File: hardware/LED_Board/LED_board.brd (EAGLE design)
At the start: 50 x 23 mm, 115 parts, among them J2 QWIIC_RIGHT_ANGLE, U1 IS31FL3731-SALS2

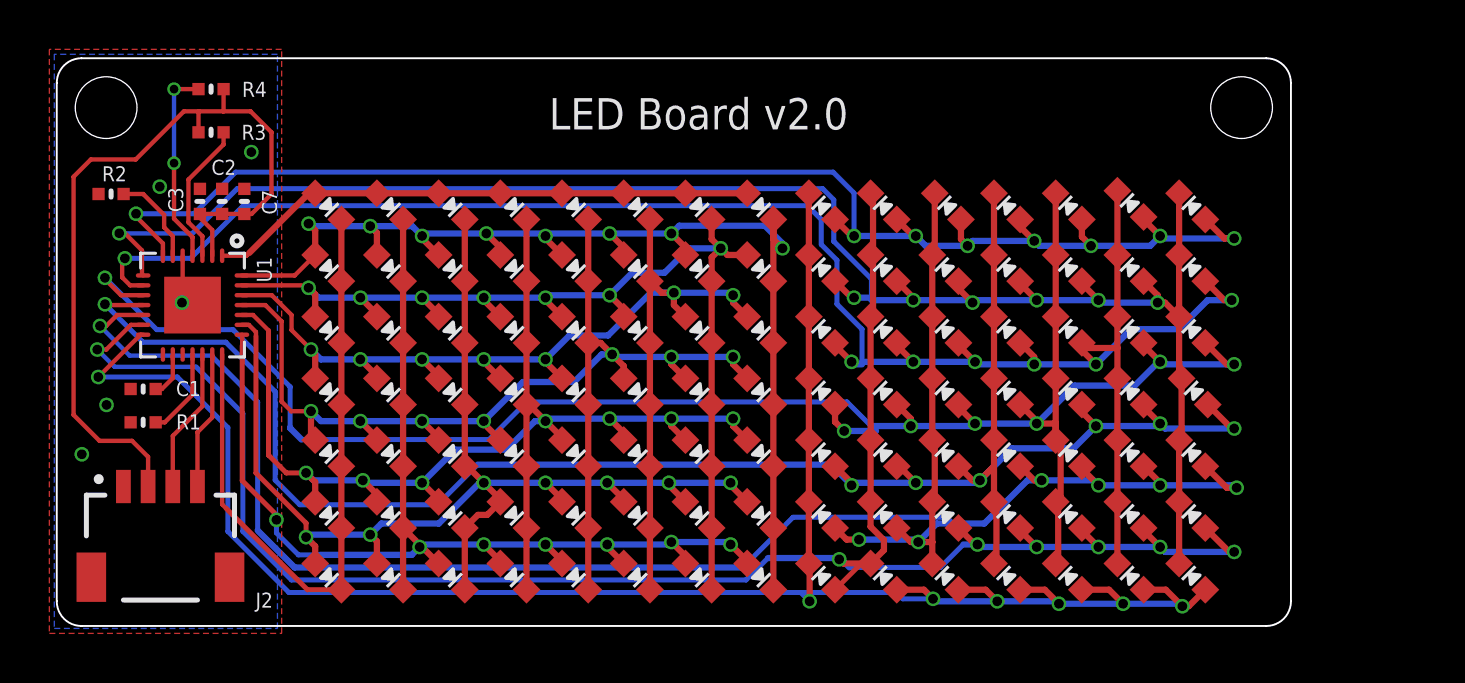
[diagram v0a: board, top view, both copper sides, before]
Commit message: LED board updated to v2.1
- Changed 0603 LEDs to 0402
- Arranged LEDs in grid of 3 x 2.5 mm spacing
- Increased board width from 50 to 55mm to accommodate spacing
- Rerouted all traces to LEDs again for new spacing (needs to be verified; v2.0 worked)
- ERC/DRC done
- Added BOM
- Updated gerbers, renders, schematic, dimensions
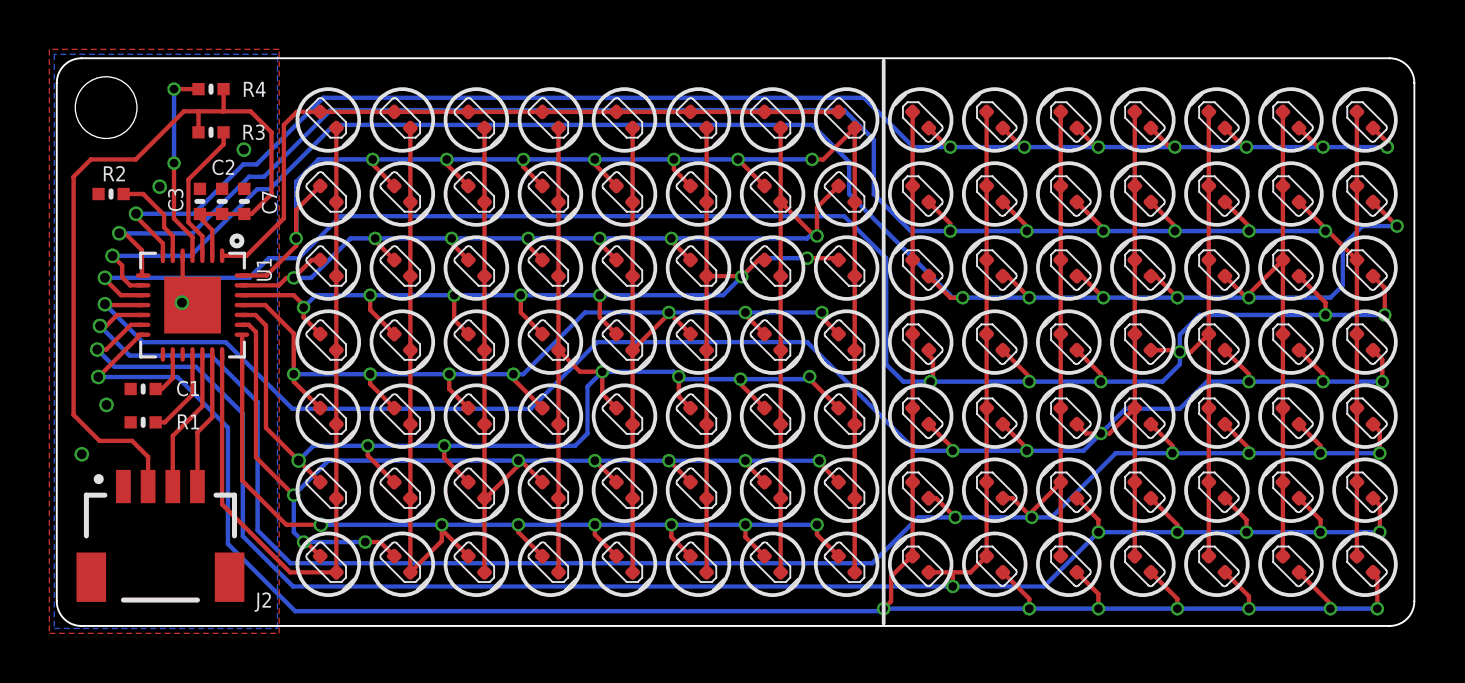
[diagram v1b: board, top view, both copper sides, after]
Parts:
- removed C1-2, C1-3, C1-4, C1-5, C1-6, C1-7, C1-8, C2-10, C2-11, C2-12, C2-13, C2-14, C2-15, C2-2, C2-3, C2-4, C2-5, C2-6, C2-7, C2-8, C2-9, C3-10, C3-11, C3-12, C3-13, C3-14, C3-15, C3-2, C3-3, C3-4, C3-5, C3-6, C3-7, C3-8, C3-9, C4-10, C4-11, C4-12, C4-13, C4-14, C4-15, C4-2, C4-3, C4-4, C4-5, C4-6, C4-7, C4-8, C4-9, C5-10, C5-11, C5-12, C5-13, C5-14, C5-15, C5-2, C5-3, C5-4, C5-5, C5-6, C5-7, C5-8, C5-9, C6-10, C6-11, C6-12, C6-13, C6-14, C6-15, C6-2, C6-3, C6-4, C6-5, C6-6, C6-7, C6-8, C6-9, C7-10, C7-11, C7-12, C7-13, C7-14, C7-15, C7-2, C7-3, C7-4, C7-5, C7-6, C7-7, C7-8, C7-9, C8-10, C8-11, C8-12, C8-13, C8-14, C8-15, C8-2, C8-3, C8-4, C8-5, C8-6, C8-7, C8-8, C8-9: (no value), microbuilder:CHIPLED_0603_NOOUTLINE
- added LED1, LED10, LED100, LED101, LED102, LED103, LED104, LED105, LED11, LED12, LED13, LED14, LED15, LED16, LED17, LED18, LED19, LED2, LED20, LED21, LED22, LED23, LED24, LED25, LED26, LED27, LED28, LED29, LED3, LED30, LED31, LED32, LED33, LED34, LED35, LED36, LED37, LED38, LED39, LED4, LED40, LED41, LED42, LED43, LED44, LED45, LED46, LED47, LED48, LED49, LED5, LED50, LED51, LED52, LED53, LED54, LED55, LED56, LED57, LED58, LED59, LED6, LED60, LED61, LED62, LED63, LED64, LED65, LED66, LED67, LED68, LED69, LED7, LED70, LED71, LED72, LED73, LED74, LED75, LED76, LED77, LED78, LED79, LED8, LED80, LED81, LED82, LED83, LED84, LED85, LED86, LED87, LED88, LED89, LED9, LED90, LED91, LED92, LED93, LED94, LED95, LED96, LED97, LED98, LED99: (no value), Seeed-LED:LED-0402
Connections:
- net CA1: now also LED1.-, LED2.-, LED3.-, LED4.-, LED5.-, LED6.-, LED7.-; no longer C1-2.C, C1-3.C, C1-4.C, C1-5.C, C1-6.C, C1-7.C, C1-8.C
- net CA2: now also LED10.-, LED11.-, LED12.-, LED13.-, LED14.-, LED15.+, LED22.+, LED29.+, LED36.+, LED43.+, LED50.+, LED8.-, LED9.-; no longer C2-2.C, C2-3.C, C2-4.C, C2-5.C, C2-6.C, C2-7.C, C2-8.C, C3-2.A, C4-2.A, C5-2.A, C6-2.A, C7-2.A, C8-2.A
- net CA3: now also LED1.+, LED15.-, LED16.-, LED17.-, LED18.-, LED19.-, LED20.-, LED21.-, LED23.+, LED30.+, LED37.+, LED44.+, LED51.+, LED8.+; no longer C1-2.A, C2-2.A, C3-2.C, C3-3.C, C3-4.C, C3-5.C, C3-6.C, C3-7.C, C3-8.C, C4-3.A, C5-3.A, C6-3.A, C7-3.A, C8-3.A
- net CA4: now also LED16.+, LED2.+, LED22.-, LED23.-, LED24.-, LED25.-, LED26.-, LED27.-, LED28.-, LED31.+, LED38.+, LED45.+, LED52.+, LED9.+; no longer C1-3.A, C2-3.A, C3-3.A, C4-2.C, C4-3.C, C4-4.C, C4-5.C, C4-6.C, C4-7.C, C4-8.C, C5-4.A, C6-4.A, C7-4.A, C8-4.A
- net CA5: now also LED10.+, LED17.+, LED24.+, LED29.-, LED3.+, LED30.-, LED31.-, LED32.-, LED33.-, LED34.-, LED35.-, LED39.+, LED46.+, LED53.+; no longer C1-4.A, C2-4.A, C3-4.A, C4-4.A, C5-2.C, C5-3.C, C5-4.C, C5-5.C, C5-6.C, C5-7.C, C5-8.C, C6-5.A, C7-5.A, C8-5.A
- net CA6: now also LED11.+, LED18.+, LED25.+, LED32.+, LED36.-, LED37.-, LED38.-, LED39.-, LED4.+, LED40.-, LED41.-, LED42.-, LED47.+, LED54.+; no longer C1-5.A, C2-5.A, C3-5.A, C4-5.A, C5-5.A, C6-2.C, C6-3.C, C6-4.C, C6-5.C, C6-6.C, C6-7.C, C6-8.C, C7-6.A, C8-6.A
- net CA7: now also LED12.+, LED19.+, LED26.+, LED33.+, LED40.+, LED43.-, LED44.-, LED45.-, LED46.-, LED47.-, LED48.-, LED49.-, LED5.+, LED55.+; no longer C1-6.A, C2-6.A, C3-6.A, C4-6.A, C5-6.A, C6-6.A, C7-2.C, C7-3.C, C7-4.C, C7-5.C, C7-6.C, C7-7.C, C7-8.C, C8-7.A
- net CA8: now also LED13.+, LED20.+, LED27.+, LED34.+, LED41.+, LED48.+, LED50.-, LED51.-, LED52.-, LED53.-, LED54.-, LED55.-, LED56.-, LED6.+; no longer C1-7.A, C2-7.A, C3-7.A, C4-7.A, C5-7.A, C6-7.A, C7-7.A, C8-2.C, C8-3.C, C8-4.C, C8-5.C, C8-6.C, C8-7.C, C8-8.C
- net CA9: now also LED14.+, LED21.+, LED28.+, LED35.+, LED42.+, LED49.+, LED56.+, LED7.+; no longer C1-8.A, C2-8.A, C3-8.A, C4-8.A, C5-8.A, C6-8.A, C7-8.A, C8-8.A
- net CB1: now also LED57.+, LED64.+, LED71.+, LED78.+, LED85.+, LED92.+, LED99.+; no longer C2-9.A, C3-9.A, C4-9.A, C5-9.A, C6-9.A, C7-9.A, C8-9.A
- net CB2: now also LED100.-, LED101.-, LED102.-, LED103.-, LED104.-, LED105.-, LED58.+, LED65.+, LED72.+, LED79.+, LED86.+, LED93.+, LED99.-; no longer C2-10.C, C2-11.C, C2-12.C, C2-13.C, C2-14.C, C2-15.C, C2-9.C, C3-10.A, C4-10.A, C5-10.A, C6-10.A, C7-10.A, C8-10.A
- net CB3: now also LED100.+, LED59.+, LED66.+, LED73.+, LED80.+, LED87.+, LED92.-, LED93.-, LED94.-, LED95.-, LED96.-, LED97.-, LED98.-; no longer C2-10.A, C3-10.C, C3-11.C, C3-12.C, C3-13.C, C3-14.C, C3-15.C, C3-9.C, C4-11.A, C5-11.A, C6-11.A, C7-11.A, C8-11.A
- net CB4: now also LED101.+, LED60.+, LED67.+, LED74.+, LED81.+, LED85.-, LED86.-, LED87.-, LED88.-, LED89.-, LED90.-, LED91.-, LED94.+; no longer C2-11.A, C3-11.A, C4-10.C, C4-11.C, C4-12.C, C4-13.C, C4-14.C, C4-15.C, C4-9.C, C5-12.A, C6-12.A, C7-12.A, C8-12.A
- net CB5: now also LED102.+, LED61.+, LED68.+, LED75.+, LED78.-, LED79.-, LED80.-, LED81.-, LED82.-, LED83.-, LED84.-, LED88.+, LED95.+; no longer C2-12.A, C3-12.A, C4-12.A, C5-10.C, C5-11.C, C5-12.C, C5-13.C, C5-14.C, C5-15.C, C5-9.C, C6-13.A, C7-13.A, C8-13.A
- net CB6: now also LED103.+, LED62.+, LED69.+, LED71.-, LED72.-, LED73.-, LED74.-, LED75.-, LED76.-, LED77.-, LED82.+, LED89.+, LED96.+; no longer C2-13.A, C3-13.A, C4-13.A, C5-13.A, C6-10.C, C6-11.C, C6-12.C, C6-13.C, C6-14.C, C6-15.C, C6-9.C, C7-14.A, C8-14.A
- net CB7: now also LED104.+, LED63.+, LED64.-, LED65.-, LED66.-, LED67.-, LED68.-, LED69.-, LED70.-, LED76.+, LED83.+, LED90.+, LED97.+; no longer C2-14.A, C3-14.A, C4-14.A, C5-14.A, C6-14.A, C7-10.C, C7-11.C, C7-12.C, C7-13.C, C7-14.C, C7-15.C, C7-9.C, C8-15.A
- net CB8: now also LED105.+, LED57.-, LED58.-, LED59.-, LED60.-, LED61.-, LED62.-, LED63.-, LED70.+, LED77.+, LED84.+, LED91.+, LED98.+; no longer C2-15.A, C3-15.A, C4-15.A, C5-15.A, C6-15.A, C7-15.A, C8-10.C, C8-11.C, C8-12.C, C8-13.C, C8-14.C, C8-15.C, C8-9.C
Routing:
- net CB2: track 71.8 -> 85.8 mm
- net CB3: track 77.6 -> 90.9 mm
- net CB8: track 80.0 -> 92.8 mm, vias 7 -> 8
- net CB4: track 78.7 -> 91.1 mm
- net CA3: track 51.1 -> 63.0 mm, vias 7 -> 8
- net CA4: track 50.6 -> 62.3 mm
- net CB7: track 80.7 -> 91.7 mm
- net CA2: track 50.0 -> 60.2 mm
- net CB5: track 77.6 -> 87.8 mm
- net CA8: track 47.9 -> 57.9 mm
- net CA7: track 43.8 -> 53.7 mm
- net CA5: track 48.8 -> 57.5 mm
- net CA6: track 46.4 -> 54.9 mm
- net CB6: track 83.8 -> 91.4 mm
- net CA9: track 22.3 -> 29.6 mm
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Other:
- board size 50 x 23 mm -> 55 x 23 mm
- board text added: "Designed by Akram Ali v2.1 | 2024-05-08"
- board text removed: "Designed by Akram Ali v2.0 | 2023-12-04"
- board text removed: "LED Board v2.0"
